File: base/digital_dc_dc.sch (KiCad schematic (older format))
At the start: 0 parts

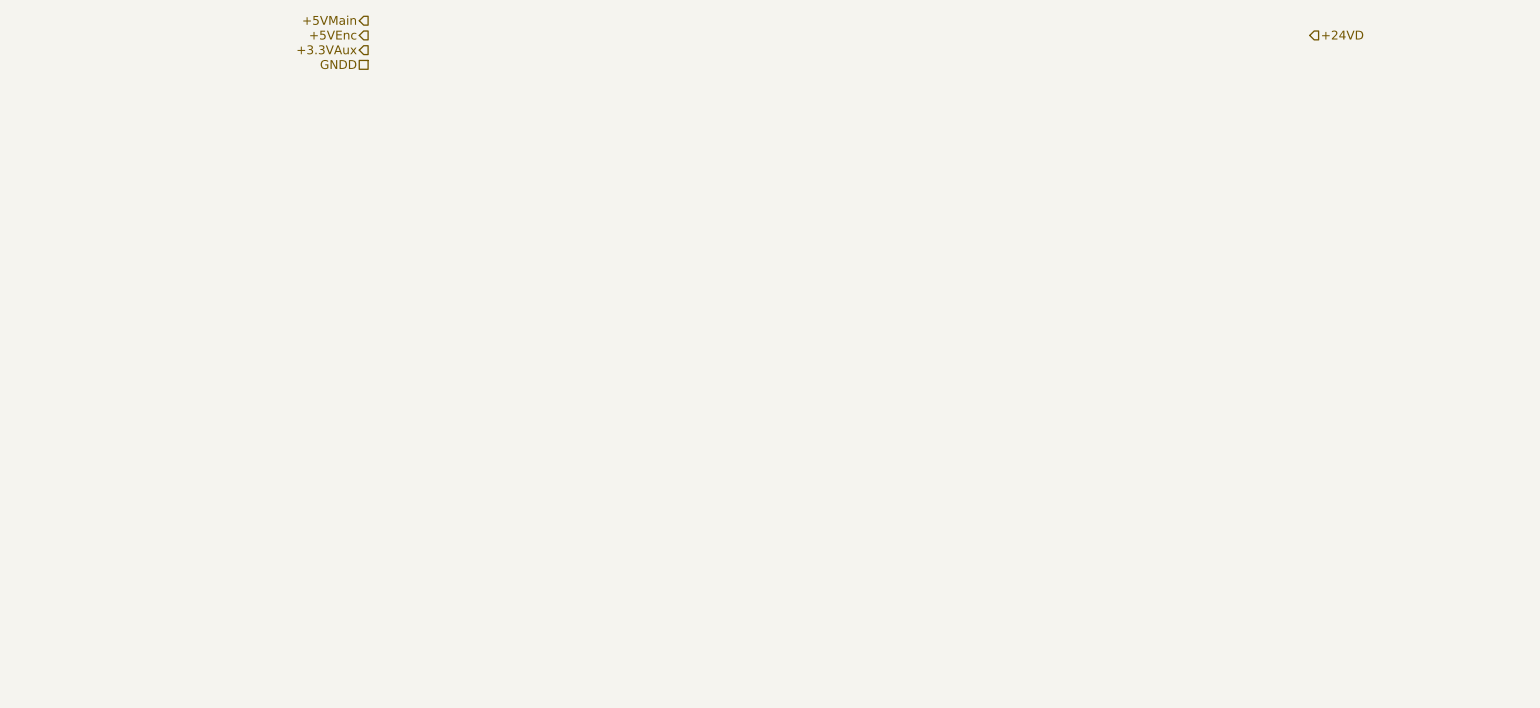
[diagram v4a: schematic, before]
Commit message: Implement digital DC/DC convertor page.
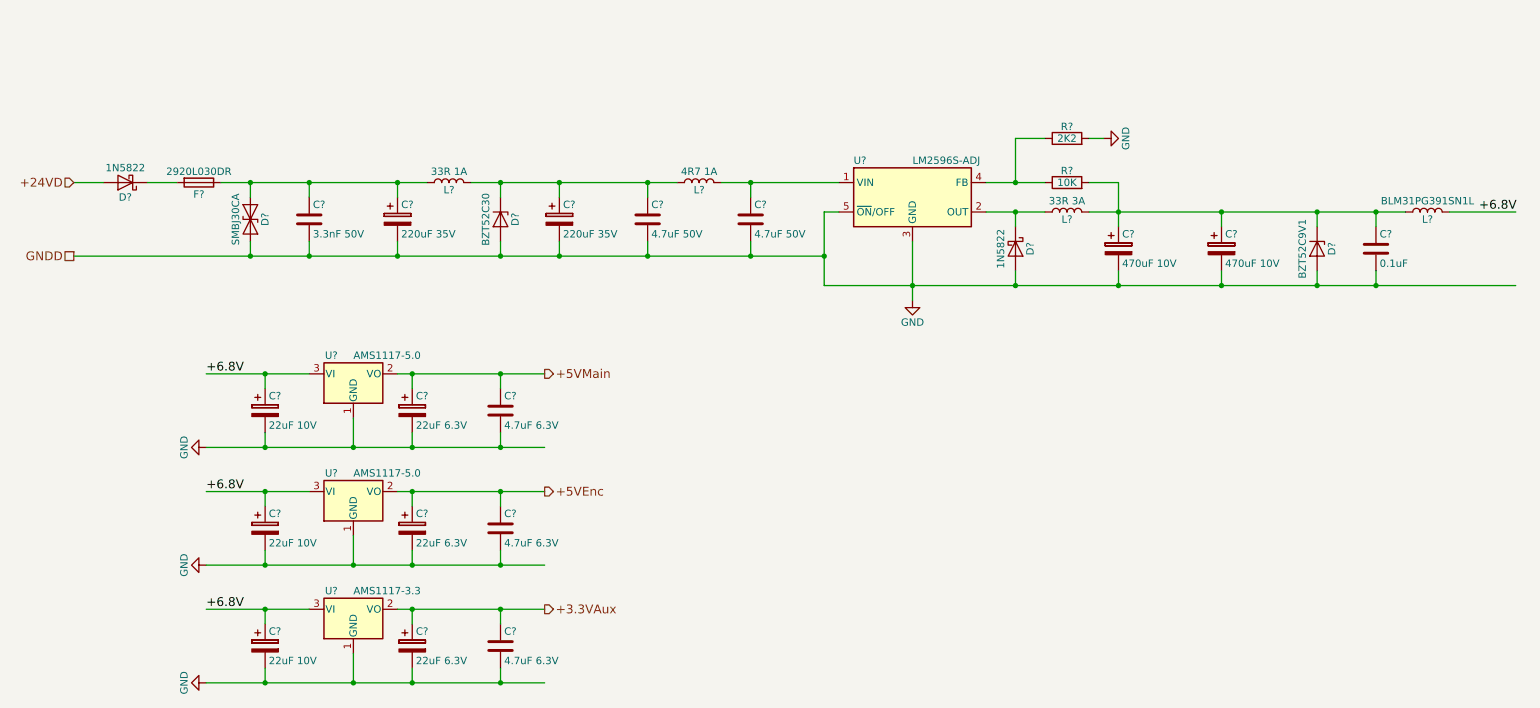
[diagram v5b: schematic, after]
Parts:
- added C?: 3.3nF 50V, Capacitor_SMD:C_0603_1608Metric, symbol C
- added C? (x2): 220uF 35V, Capacitor_SMD:CP_Elec_8x10, symbol CP
- added C? (x2): 4.7uF 50V, Capacitor_SMD:C_1210_3225Metric, symbol C
- added C? (x2): 470uF 10V, Capacitor_SMD:CP_Elec_8x10, symbol CP
- added C?: 0.1uF, Capacitor_SMD:C_0603_1608Metric, symbol C
- added C? (x3): 22uF 10V, Capacitor_Tantalum_SMD:CP_EIA-3216-18_Kemet-A, symbol CP
- added C? (x3): 22uF 6.3V, Capacitor_Tantalum_SMD:CP_EIA-3216-18_Kemet-A, symbol CP
- added C? (x3): 4.7uF 6.3V, Capacitor_SMD:C_0603_1608Metric, symbol C
- added D? (x2): 1N5822, Diode_SMD:D_SMA, symbol 1N5822
- added D?: SMBJ30CA, Diode_SMD:D_SMB, symbol D_TVS
- added D?: BZT52C30, Diode_SMD:D_SOD-123, symbol D_Zener
- added D?: BZT52C9V1, Diode_SMD:D_SOD-123, symbol D_Zener
- added F?: 2920L030DR, Fuse:Fuse_2920_7451Metric, symbol Fuse
- added L?: 33R 1A, Inductor_SMD:L_7.3x7.3_H3.5, symbol L
- added L?: 4R7 1A, Inductor_SMD:L_Taiyo-Yuden_MD-3030, symbol L
- added L?: 33R 3A, Inductor_SMD:L_12x12mm_h8mm, symbol L
- added L?: BLM31PG391SN1L, Inductor_SMD:L_1206_3216Metric, symbol L
- added R?: 10K, Resistor_SMD:R_0603_1608Metric, symbol R
- added R?: 2K2, Resistor_SMD:R_0603_1608Metric, symbol R
- added U?: LM2596S-ADJ, Package_TO_SOT_SMD:TO-263-5_TabPin3, symbol LM2596S-ADJ
- added U? (x2): AMS1117-5.0, Package_TO_SOT_SMD:SOT-223, symbol AP1117-15
- added U?: AMS1117-3.3, Package_TO_SOT_SMD:SOT-223, symbol AP1117-15
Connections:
- net labels added: +6.8V, GND
- wire segments 0 -> 72

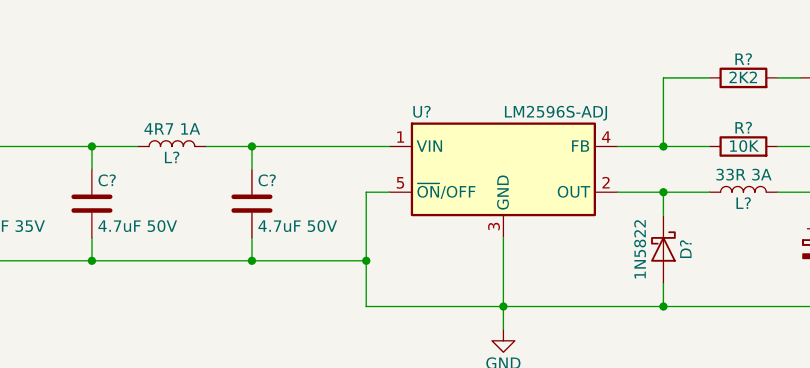
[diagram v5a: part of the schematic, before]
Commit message: 1. Separate dio_can_rs485 sheet into two: dio + can_rs485. 2. Move can and rs485 into digital power domain 3. Add CAN transiever to can_rs485 sheet
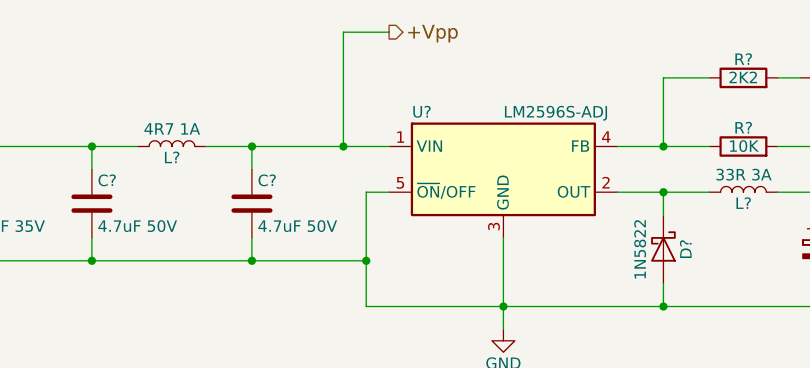
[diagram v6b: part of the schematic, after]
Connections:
- net labels added: +Vpp
- wire segments 72 -> 74
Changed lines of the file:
@@
 LIBS:dc-dc
 LIBS:regul
+LIBS:interface
+LIBS:ESD_Protection
 LIBS:4hbd-base-cache
 EELAYER 25 0
@@
 $Descr A4 11693 8268
 encoding utf-8
-Sheet 6 8
+Sheet 6 9
 Title ""
 Date ""
@@
 Connection ~ 9000 3200
 Connection ~ 10050 3700
+Text HLabel 6400 2500 2    60   Output ~ 0
++Vpp
+Wire Wire Line
+	6200 3000 6200 2500
+Wire Wire Line
+	6200 2500 6400 2500
+Connection ~ 6200 3000
 $EndSCHEMATC
